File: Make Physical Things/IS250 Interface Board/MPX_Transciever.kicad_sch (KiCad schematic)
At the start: 12 parts, among them Q3 PN2222A, Q4 PN2222A, Q5 PN2222A, Q6 PN2222A

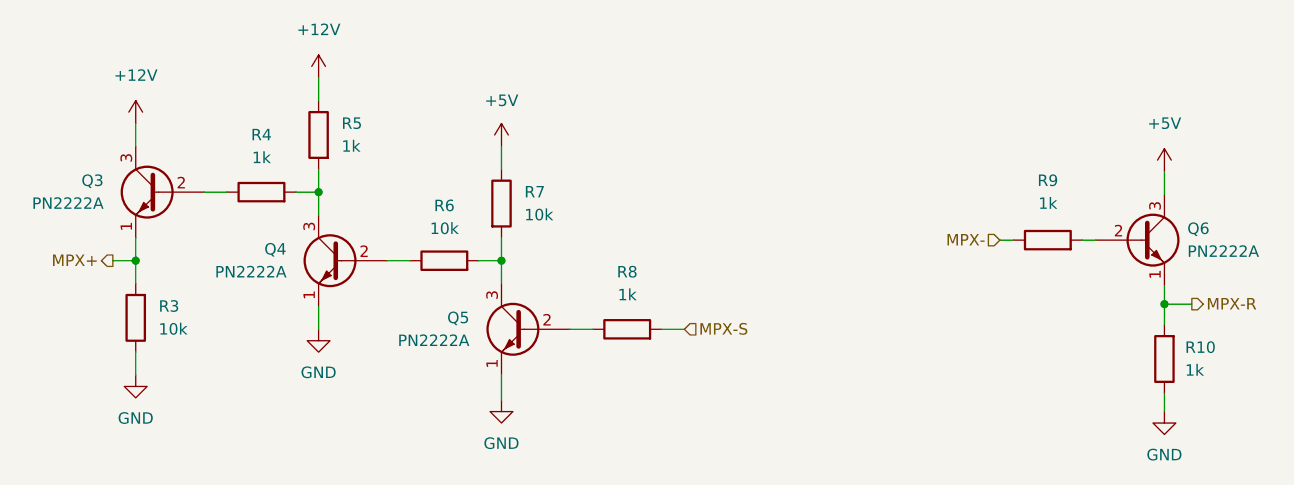
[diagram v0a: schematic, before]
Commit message: Updated Components to have footprints
Added footprints to components that had the wrong ones or were completely missing
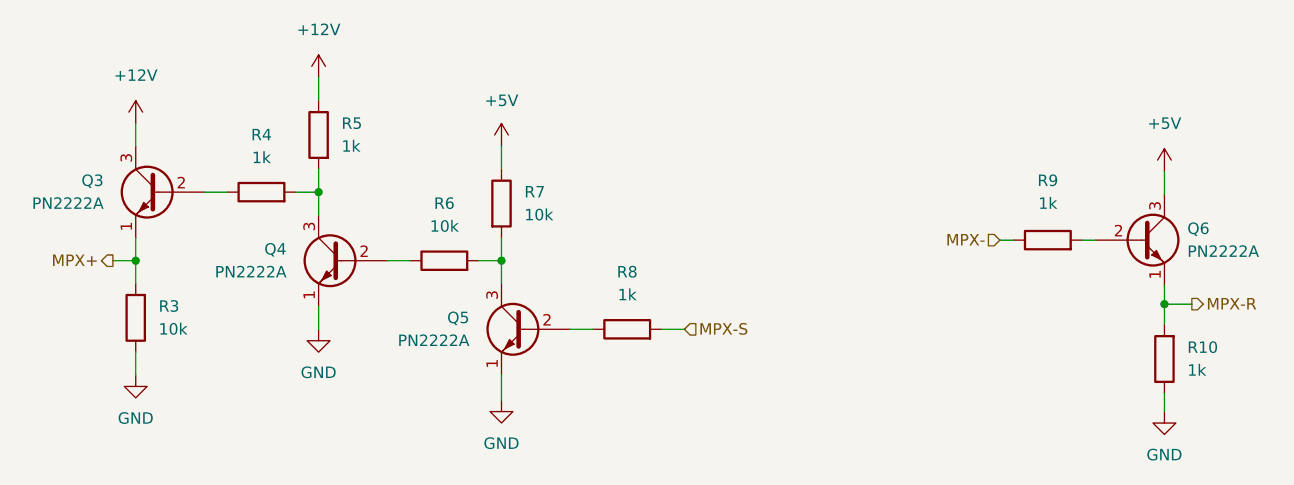
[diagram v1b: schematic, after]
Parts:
- R10, R3, R4, R5, R6, R7, R8, R9: footprint (none) -> Resistor_THT:R_Axial_DIN0207_L6.3mm_D2.5mm_P10.16mm_Horizontal
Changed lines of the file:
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@@
     (property "Reference" "R8" (id 0) (at 97.79 52.07 90))
     (property "Value" "1k" (id 1) (at 97.79 54.61 90))
-    (property "Footprint" "" (id 2) (at 97.79 60.198 90)
+    (property "Footprint" "Resistor_THT:R_Axial_DIN0207_L6.3mm_D2.5mm_P10.16mm_Horizontal" (id 2) (at 97.79 60.198 90)
       (effects (font (size 1.27 1.27)) hide)
     )
@@
       (effects (font (size 1.27 1.27)) (justify right))
     )
-    (property "Footprint" "" (id 2) (at 44.958 57.15 90)
+    (property "Footprint" "Resistor_THT:R_Axial_DIN0207_L6.3mm_D2.5mm_P10.16mm_Horizontal" (id 2) (at 44.958 57.15 90)
       (effects (font (size 1.27 1.27)) hide)
     )
@@
   (symbol (lib_id "Device:R") (at 77.47 50.8 90) (unit 1)
     (in_bom yes) (on_board yes) (fields_autoplaced)
-    (property "Reference" "R6" (id 0) (at 77.47 44.704 90))
-    (property "Value" "10k" (id 1) (at 77.47 47.244 90))
-    (property "Footprint" "" (id 2) (at 77.47 52.578 90)
+    (property "Reference" "R6" (id 0) (at 77.47 44.45 90))
+    (property "Value" "10k" (id 1) (at 77.47 46.99 90))
+    (property "Footprint" "Resistor_THT:R_Axial_DIN0207_L6.3mm_D2.5mm_P10.16mm_Horizontal" (id 2) (at 77.47 52.578 90)
       (effects (font (size 1.27 1.27)) hide)
     )
@@
     (property "Reference" "R4" (id 0) (at 57.15 36.83 90))
     (property "Value" "1k" (id 1) (at 57.15 39.37 90))
-    (property "Footprint" "" (id 2) (at 57.15 44.958 90)
+    (property "Footprint" "Resistor_THT:R_Axial_DIN0207_L6.3mm_D2.5mm_P10.16mm_Horizontal" (id 2) (at 57.15 44.958 90)
       (effects (font (size 1.27 1.27)) hide)
     )
@@
   (symbol (lib_id "Device:R") (at 157.48 61.722 180) (unit 1)
     (in_bom yes) (on_board yes) (fields_autoplaced)
-    (property "Reference" "R10" (id 0) (at 159.766 60.4519 0)
-      (effects (font (size 1.27 1.27)) (justify right))
-    )
-    (property "Value" "1k" (id 1) (at 159.766 62.9919 0)
-      (effects (font (size 1.27 1.27)) (justify right))
-    )
-    (property "Footprint" "" (id 2) (at 159.258 61.722 90)
+    (property "Reference" "R10" (id 0) (at 160.02 60.4519 0)
+      (effects (font (size 1.27 1.27)) (justify right))
+    )
+    (property "Value" "1k" (id 1) (at 160.02 62.9919 0)
+      (effects (font (size 1.27 1.27)) (justify right))
+    )
+    (property "Footprint" "Resistor_THT:R_Axial_DIN0207_L6.3mm_D2.5mm_P10.16mm_Horizontal" (id 2) (at 159.258 61.722 90)
       (effects (font (size 1.27 1.27)) hide)
     )
@@
     (property "Reference" "R9" (id 0) (at 144.526 41.91 90))
     (property "Value" "1k" (id 1) (at 144.526 44.45 90))
-    (property "Footprint" "" (id 2) (at 144.526 50.292 90)
+    (property "Footprint" "Resistor_THT:R_Axial_DIN0207_L6.3mm_D2.5mm_P10.16mm_Horizontal" (id 2) (at 144.526 50.292 90)
       (effects (font (size 1.27 1.27)) hide)
     )
@@
       (effects (font (size 1.27 1.27)) (justify right))
     )
-    (property "Footprint" "" (id 2) (at 65.278 36.83 90)
+    (property "Footprint" "Resistor_THT:R_Axial_DIN0207_L6.3mm_D2.5mm_P10.16mm_Horizontal" (id 2) (at 65.278 36.83 90)
       (effects (font (size 1.27 1.27)) hide)
     )
@@
       (effects (font (size 1.27 1.27)) (justify left))
     )
-    (property "Footprint" "" (id 2) (at 82.042 44.45 90)
-      (effects (font (size 1.27 1.27)) hide)
-    )
+    (property "Footprint" "Resistor_THT:R_Axial_DIN0207_L6.3mm_D2.5mm_P10.16mm_Horizontal" (id 2) (at 82.042 44.45 90)
+      (effects (font (size 1.27 1.27)) hide)
+    )
